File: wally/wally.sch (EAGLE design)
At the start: 2 parts, among them IC1 ESP32-S3-WROOM-1-N4, U1 RA-01H

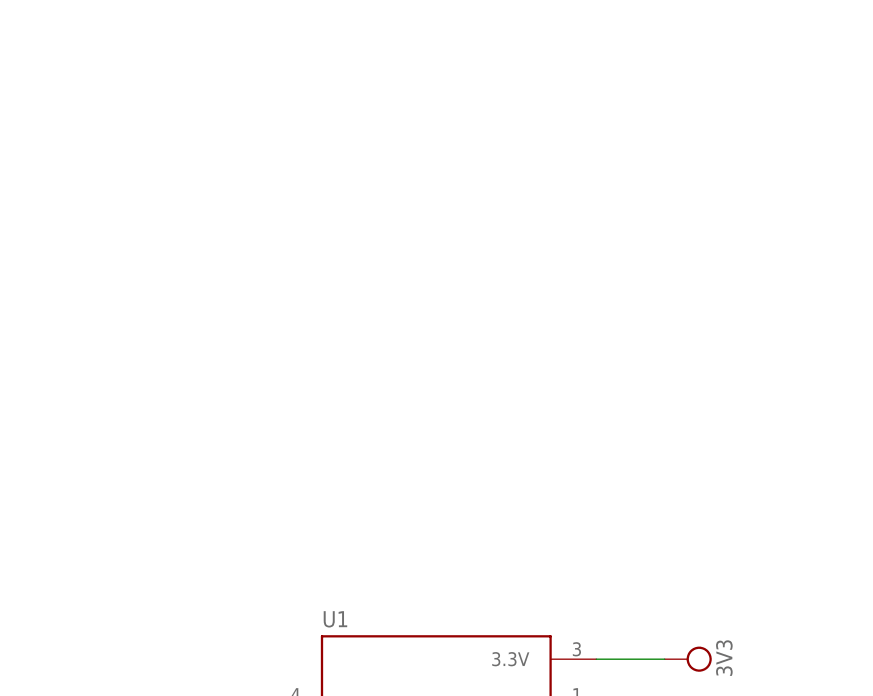
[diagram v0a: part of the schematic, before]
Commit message: usb c port
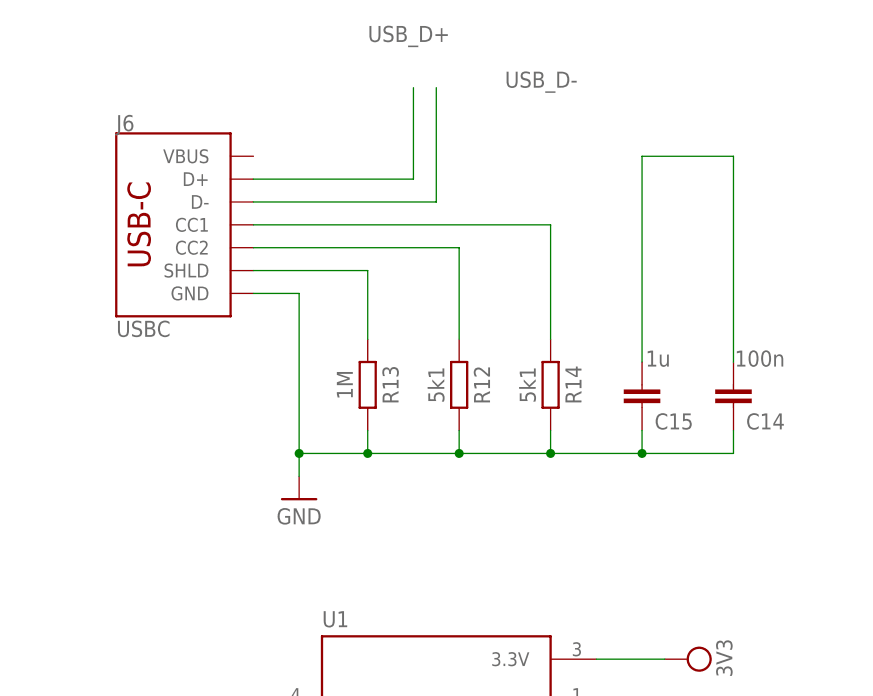
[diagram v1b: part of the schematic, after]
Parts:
- added C14: 100n, Capacitor:C_CHIP-0603(1608-METRIC)
- added C15: 1u, Capacitor:C_CHIP-0603(1608-METRIC)
- added J6: USBC, SparkFun-Connectors:USB_C_2-LAYER_PADS
- added R12, R14: 5k1, Resistor:R_CHIP-0603(1608-METRIC)
- added R13: 1M, Resistor:R_CHIP-0603(1608-METRIC)
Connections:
- new net N$21: J6.SHLD, R13.1
- new net N$24: J6.CC2, R12.1
- new net N$25: J6.CC1, R14.1
- new net N$26: C14.2, C15.2
- new net USB_D+: J6.D+
- new net USB_D-: J6.D-
- net GND: now also C14.1, C15.1, J6.GND, R12.2, R13.2, R14.2
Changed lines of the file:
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@@
 <part name="SUPPLY4" library="Power_Symbols" library_urn="urn:adsk.eagle:library:16502351" deviceset="3V3-CIRCLE" device="" value="3V3"/>
 <part name="SUPPLY5" library="Power_Symbols" library_urn="urn:adsk.eagle:library:16502351" deviceset="3V3-CIRCLE" device="" value="3V3"/>
+<part name="J6" library="SparkFun-Connectors" deviceset="USB_C" device="_2-LAYER_PADS" override_package3d_urn="urn:adsk.eagle:package:44095805/2" override_package_urn="urn:adsk.eagle:footprint:44095806/1" value="USBC"/>
+<part name="SUPPLY24" library="Power_Symbols" library_urn="urn:adsk.eagle:library:16502351" deviceset="GND-BAR" device="" value="GND"/>
+<part name="R12" library="Resistor" library_urn="urn:adsk.eagle:library:16378527" deviceset="R" device="CHIP-0603(1608-METRIC)" package3d_urn="urn:adsk.eagle:package:16378565/5" technology="_" value="5k1"/>
+<part name="R13" library="Resistor" library_urn="urn:adsk.eagle:library:16378527" deviceset="R" device="CHIP-0603(1608-METRIC)" package3d_urn="urn:adsk.eagle:package:16378565/5" technology="_" value="1M"/>
+<part name="R14" library="Resistor" library_urn="urn:adsk.eagle:library:16378527" deviceset="R" device="CHIP-0603(1608-METRIC)" package3d_urn="urn:adsk.eagle:package:16378565/5" technology="_" value="5k1"/>
+<part name="C14" library="Capacitor" library_urn="urn:adsk.eagle:library:16290819" deviceset="C" device="CHIP-0603(1608-METRIC)" package3d_urn="urn:adsk.eagle:package:16290898/5" technology="_" value="100n"/>
+<part name="C15" library="Capacitor" library_urn="urn:adsk.eagle:library:16290819" deviceset="C" device="CHIP-0603(1608-METRIC)" package3d_urn="urn:adsk.eagle:package:16290898/5" technology="_" value="1u"/>
 </parts>
 <sheets>
@@
 <instance part="SUPPLY5" gate="G$1" x="-27.94" y="-5.08" smashed="yes" rot="R90">
 <attribute name="VALUE" x="-31.115" y="-5.207" size="1.778" layer="96" rot="R90" align="bottom-center"/>
+</instance>
+<instance part="J6" gate="J1" x="-20.32" y="106.68" smashed="yes">
+<attribute name="VALUE" x="-22.86" y="94.234" size="1.778" layer="96" font="vector" rot="MR180" align="top-left"/>
+<attribute name="NAME" x="-22.86" y="117.094" size="1.778" layer="95" font="vector"/>
+</instance>
+<instance part="SUPPLY24" gate="G$1" x="-2.54" y="76.2" smashed="yes">
+<attribute name="VALUE" x="-2.54" y="74.295" size="1.778" layer="96" align="center"/>
+</instance>
+<instance part="R12" gate="G$1" x="15.24" y="88.9" smashed="yes" rot="R270">
+<attribute name="NAME" x="17.78" y="88.9" size="1.778" layer="95" rot="R270" align="center"/>
+<attribute name="VALUE" x="12.7" y="88.9" size="1.778" layer="96" rot="R270" align="center"/>
+</instance>
+<instance part="R13" gate="G$1" x="5.08" y="88.9" smashed="yes" rot="R270">
+<attribute name="NAME" x="7.62" y="88.9" size="1.778" layer="95" rot="R270" align="center"/>
+<attribute name="VALUE" x="2.54" y="88.9" size="1.778" layer="96" rot="R270" align="center"/>
+</instance>
+<instance part="R14" gate="G$1" x="25.4" y="88.9" smashed="yes" rot="R270">
+<attribute name="NAME" x="27.94" y="88.9" size="1.778" layer="95" rot="R270" align="center"/>
+<attribute name="VALUE" x="22.86" y="88.9" size="1.778" layer="96" rot="R270" align="center"/>
+</instance>
+<instance part="C14" gate="G$1" x="45.72" y="86.36" smashed="yes" rot="R180">
+<attribute name="NAME" x="51.435" y="85.725" size="1.778" layer="95" rot="R180"/>
+<attribute name="VALUE" x="51.435" y="92.71" size="1.778" layer="96" rot="R180"/>
+</instance>
+<instance part="C15" gate="G$1" x="35.56" y="86.36" smashed="yes" rot="R180">
+<attribute name="NAME" x="41.275" y="85.725" size="1.778" layer="95" rot="R180"/>
+<attribute name="VALUE" x="38.735" y="92.71" size="1.778" layer="96" rot="R180"/>
 </instance>
 </instances>
@@
 <junction x="33.02" y="-60.96"/>
 </segment>
+<segment>
+<pinref part="J6" gate="J1" pin="GND"/>
+<wire x1="-7.62" y1="99.06" x2="-2.54" y2="99.06" width="0.1524" layer="91"/>
+<pinref part="SUPPLY24" gate="G$1" pin="GND"/>
+<wire x1="-2.54" y1="99.06" x2="-2.54" y2="81.28" width="0.1524" layer="91"/>
+<pinref part="R13" gate="G$1" pin="2"/>
+<wire x1="-2.54" y1="81.28" x2="-2.54" y2="78.74" width="0.1524" layer="91"/>
+<wire x1="5.08" y1="83.82" x2="5.08" y2="81.28" width="0.1524" layer="91"/>
+<wire x1="5.08" y1="81.28" x2="-2.54" y2="81.28" width="0.1524" layer="91"/>
+<junction x="-2.54" y="81.28"/>
+<pinref part="R14" gate="G$1" pin="2"/>
+<wire x1="25.4" y1="83.82" x2="25.4" y2="81.28" width="0.1524" layer="91"/>
+<wire x1="25.4" y1="81.28" x2="15.24" y2="81.28" width="0.1524" layer="91"/>
+<junction x="5.08" y="81.28"/>
+<pinref part="R12" gate="G$1" pin="2"/>
+<wire x1="15.24" y1="81.28" x2="5.08" y2="81.28" width="0.1524" layer="91"/>
+<wire x1="15.24" y1="83.82" x2="15.24" y2="81.28" width="0.1524" layer="91"/>
+<junction x="15.24" y="81.28"/>
+<pinref part="C15" gate="G$1" pin="1"/>
+<wire x1="35.56" y1="83.82" x2="35.56" y2="81.28" width="0.1524" layer="91"/>
+<wire x1="35.56" y1="81.28" x2="25.4" y2="81.28" width="0.1524" layer="91"/>
+<junction x="25.4" y="81.28"/>
+<pinref part="C14" gate="G$1" pin="1"/>
+<wire x1="45.72" y1="83.82" x2="45.72" y2="81.28" width="0.1524" layer="91"/>
+<wire x1="45.72" y1="81.28" x2="35.56" y2="81.28" width="0.1524" layer="91"/>
+<junction x="35.56" y="81.28"/>
+</segment>
 </net>
 <net name="3V3" class="0">
@@
 <pinref part="U1" gate="G$1" pin="3.3V"/>
 <wire x1="38.1" y1="58.42" x2="30.48" y2="58.42" width="0.1524" layer="91"/>
+</segment>
+</net>
+<net name="N$21" class="0">
+<segment>
+<pinref part="J6" gate="J1" pin="SHLD"/>
+<pinref part="R13" gate="G$1" pin="1"/>
+<wire x1="-7.62" y1="101.6" x2="5.08" y2="101.6" width="0.1524" layer="91"/>
+<wire x1="5.08" y1="101.6" x2="5.08" y2="93.98" width="0.1524" layer="91"/>
+</segment>
+</net>
+<net name="N$24" class="0">
+<segment>
+<pinref part="J6" gate="J1" pin="CC2"/>
+<wire x1="-7.62" y1="104.14" x2="15.24" y2="104.14" width="0.1524" layer="91"/>
+<pinref part="R12" gate="G$1" pin="1"/>
+<wire x1="15.24" y1="104.14" x2="15.24" y2="93.98" width="0.1524" layer="91"/>
+</segment>
+</net>
+<net name="N$25" class="0">
+<segment>
+<pinref part="J6" gate="J1" pin="CC1"/>
+<pinref part="R14" gate="G$1" pin="1"/>
+<wire x1="-7.62" y1="106.68" x2="25.4" y2="106.68" width="0.1524" layer="91"/>
+<wire x1="25.4" y1="106.68" x2="25.4" y2="93.98" width="0.1524" layer="91"/>
+</segment>
+</net>
+<net name="N$26" class="0">
+<segment>
+<pinref part="C14" gate="G$1" pin="2"/>
+<wire x1="35.56" y1="114.3" x2="45.72" y2="114.3" width="0.1524" layer="91"/>
+<wire x1="45.72" y1="114.3" x2="45.72" y2="91.44" width="0.1524" layer="91"/>
+<pinref part="C15" gate="G$1" pin="2"/>
+<wire x1="35.56" y1="91.44" x2="35.56" y2="114.3" width="0.1524" layer="91"/>
+</segment>
+</net>
+<net name="USB_D+" class="0">
+<segment>
+<pinref part="J6" gate="J1" pin="D+"/>
+<wire x1="-7.62" y1="111.76" x2="10.16" y2="111.76" width="0.1524" layer="91"/>
+<wire x1="10.16" y1="111.76" x2="10.16" y2="121.92" width="0.1524" layer="91"/>
+<label x="5.08" y="127" size="1.778" layer="95"/>
+</segment>
+</net>
+<net name="USB_D-" class="0">
+<segment>
+<pinref part="J6" gate="J1" pin="D-"/>
+<wire x1="-7.62" y1="109.22" x2="12.7" y2="109.22" width="0.1524" layer="91"/>
+<wire x1="12.7" y1="109.22" x2="12.7" y2="121.92" width="0.1524" layer="91"/>
+<label x="20.32" y="121.92" size="1.778" layer="95"/>
 </segment>
 </net>
@@
 will not be understood (or retained) with this version.
 </note>
+<note version="8.3" severity="warning">
+Since Version 8.3, EAGLE supports the association of 3D packages
+with devices in libraries, schematics, and board files. Those 3D
+packages will not be understood (or retained) with this version.
+</note>
+<note version="9.4" severity="warning">
+Since Version 9.4, EAGLE supports the overriding of 3D packages
+in schematics and board files. Those overridden 3d packages
+will not be understood (or retained) with this version.
+</note>

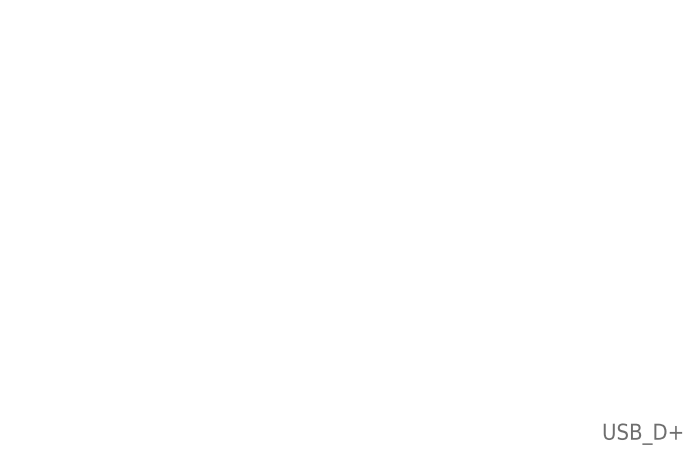
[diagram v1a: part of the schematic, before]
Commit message: SIM7600G (treat as pin header)
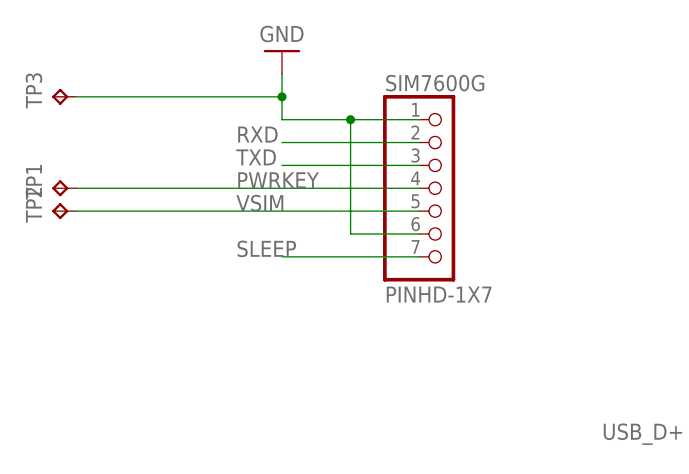
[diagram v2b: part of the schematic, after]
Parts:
- added SIM7600G: PINHD-1X7, Connector:PINHD-1X7
- added TP1, TP2, TP3: TPPAD1-13, testpad:TPPAD1-13
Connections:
- new net PWRKEY: SIM7600G.4, TP1.TP
- new net RXD: SIM7600G.2
- new net SLEEP: SIM7600G.7
- new net TXD: SIM7600G.3
- new net VSIM: SIM7600G.5, TP2.TP
- net GND: now also SIM7600G.1, SIM7600G.6, TP3.TP
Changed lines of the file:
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@@
 <part name="C14" library="Capacitor" library_urn="urn:adsk.eagle:library:16290819" deviceset="C" device="CHIP-0603(1608-METRIC)" package3d_urn="urn:adsk.eagle:package:16290898/5" technology="_" value="100n"/>
 <part name="C15" library="Capacitor" library_urn="urn:adsk.eagle:library:16290819" deviceset="C" device="CHIP-0603(1608-METRIC)" package3d_urn="urn:adsk.eagle:package:16290898/5" technology="_" value="1u"/>
+<part name="SIM7600G" library="Connector" library_urn="urn:adsk.eagle:library:16378166" deviceset="PINHD-1X7" device="" package3d_urn="urn:adsk.eagle:package:22477/2"/>
+<part name="SUPPLY6" library="Power_Symbols" library_urn="urn:adsk.eagle:library:16502351" deviceset="GND-BAR" device="" value="GND"/>
+<part name="TP1" library="testpad" library_urn="urn:adsk.eagle:library:385" deviceset="TP" device="PAD1-13" package3d_urn="urn:adsk.eagle:package:27946/1"/>
+<part name="TP2" library="testpad" library_urn="urn:adsk.eagle:library:385" deviceset="TP" device="PAD1-13" package3d_urn="urn:adsk.eagle:package:27946/1"/>
+<part name="TP3" library="testpad" library_urn="urn:adsk.eagle:library:385" deviceset="TP" device="PAD1-13" package3d_urn="urn:adsk.eagle:package:27946/1"/>
 </parts>
 <sheets>
@@
 <attribute name="NAME" x="41.275" y="85.725" size="1.778" layer="95" rot="R180"/>
 <attribute name="VALUE" x="38.735" y="92.71" size="1.778" layer="96" rot="R180"/>
+</instance>
+<instance part="SIM7600G" gate="A" x="-12.7" y="154.94" smashed="yes">
+<attribute name="NAME" x="-19.05" y="165.735" size="1.778" layer="95"/>
+<attribute name="VALUE" x="-19.05" y="142.24" size="1.778" layer="96"/>
+</instance>
+<instance part="SUPPLY6" gate="G$1" x="-30.48" y="170.18" smashed="yes" rot="R180">
+<attribute name="VALUE" x="-30.48" y="172.085" size="1.778" layer="96" rot="R180" align="center"/>
+</instance>
+<instance part="TP1" gate="G$1" x="-55.88" y="154.94" smashed="yes" rot="R90">
+<attribute name="NAME" x="-57.15" y="153.67" size="1.778" layer="95" rot="R90"/>
+<attribute name="TP_SIGNAL_NAME" x="-54.61" y="156.21" size="1.778" layer="97" rot="R90"/>
+</instance>
+<instance part="TP2" gate="G$1" x="-55.88" y="152.4" smashed="yes" rot="R90">
+<attribute name="NAME" x="-57.15" y="151.13" size="1.778" layer="95" rot="R90"/>
+<attribute name="TP_SIGNAL_NAME" x="-54.61" y="153.67" size="1.778" layer="97" rot="R90"/>
+</instance>
+<instance part="TP3" gate="G$1" x="-55.88" y="165.1" smashed="yes" rot="R90">
+<attribute name="NAME" x="-57.15" y="163.83" size="1.778" layer="95" rot="R90"/>
+<attribute name="TP_SIGNAL_NAME" x="-54.61" y="166.37" size="1.778" layer="97" rot="R90"/>
 </instance>
 </instances>
@@
 <junction x="35.56" y="81.28"/>
 </segment>
+<segment>
+<pinref part="SIM7600G" gate="A" pin="1"/>
+<wire x1="-15.24" y1="162.56" x2="-22.86" y2="162.56" width="0.1524" layer="91"/>
+<pinref part="SUPPLY6" gate="G$1" pin="GND"/>
+<wire x1="-22.86" y1="162.56" x2="-30.48" y2="162.56" width="0.1524" layer="91"/>
+<wire x1="-30.48" y1="162.56" x2="-30.48" y2="165.1" width="0.1524" layer="91"/>
+<pinref part="SIM7600G" gate="A" pin="6"/>
+<wire x1="-30.48" y1="165.1" x2="-30.48" y2="167.64" width="0.1524" layer="91"/>
+<wire x1="-15.24" y1="149.86" x2="-22.86" y2="149.86" width="0.1524" layer="91"/>
+<wire x1="-22.86" y1="149.86" x2="-22.86" y2="162.56" width="0.1524" layer="91"/>
+<junction x="-22.86" y="162.56"/>
+<pinref part="TP3" gate="G$1" pin="TP"/>
+<wire x1="-53.34" y1="165.1" x2="-30.48" y2="165.1" width="0.1524" layer="91"/>
+<junction x="-30.48" y="165.1"/>
+</segment>
 </net>
 <net name="3V3" class="0">
@@
 </segment>
 </net>
+<net name="RXD" class="0">
+<segment>
+<pinref part="SIM7600G" gate="A" pin="2"/>
+<wire x1="-15.24" y1="160.02" x2="-30.48" y2="160.02" width="0.1524" layer="91"/>
+<label x="-35.56" y="160.02" size="1.778" layer="95"/>
+</segment>
+</net>
+<net name="TXD" class="0">
+<segment>
+<pinref part="SIM7600G" gate="A" pin="3"/>
+<wire x1="-15.24" y1="157.48" x2="-30.48" y2="157.48" width="0.1524" layer="91"/>
+<label x="-35.56" y="157.48" size="1.778" layer="95"/>
+</segment>
+</net>
+<net name="PWRKEY" class="0">
+<segment>
+<pinref part="SIM7600G" gate="A" pin="4"/>
+<label x="-35.56" y="154.94" size="1.778" layer="95"/>
+<pinref part="TP1" gate="G$1" pin="TP"/>
+<wire x1="-53.34" y1="154.94" x2="-15.24" y2="154.94" width="0.1524" layer="91"/>
+</segment>
+</net>
+<net name="VSIM" class="0">
+<segment>
+<pinref part="SIM7600G" gate="A" pin="5"/>
+<label x="-35.56" y="152.4" size="1.778" layer="95"/>
+<pinref part="TP2" gate="G$1" pin="TP"/>
+<wire x1="-53.34" y1="152.4" x2="-15.24" y2="152.4" width="0.1524" layer="91"/>
+</segment>
+</net>
+<net name="SLEEP" class="0">
+<segment>
+<pinref part="SIM7600G" gate="A" pin="7"/>
+<wire x1="-15.24" y1="147.32" x2="-30.48" y2="147.32" width="0.1524" layer="91"/>
+<label x="-35.56" y="147.32" size="1.778" layer="95"/>
+</segment>
+</net>
